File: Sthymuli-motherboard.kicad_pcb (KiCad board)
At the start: 4 copper layers, 153.6 x 66.2 mm, 196 parts, among them J1 USB_C_Receptacle_USB2.0_16P, J11 Conn_02x08_Counter_Clockwise, J12 Conn_02x08_Counter_Clockwise, J2 Conn_01x09, J3 Conn_01x03, J4 Conn_01x06, J8 Conn_02x08_Counter_Clockwise, Q1 Q_NMOS_Depletion_GSD, Q2 Q_NMOS_Depletion_GSD, Q3 Q_NMOS_Depletion_GSD, Q4 Q_NMOS_Depletion_GSD, Q5 Q_NMOS_Depletion_GSD, Q6 Q_NMOS_Depletion_GSD, Q7 PMOS, Q8 NX7002AK, Q9 NX7002AK, SW1 SW_Push, SW2 SW_Push, SW3 SW_Push, SW4 SW_Push, U1 ESP32-S3-WROOM-1, U10 74HC4051, U11 MCP6L01x-xOT, U12 74HC4051, U14 LSM6DS3, U15 ITR9909, U16 ITR9909, U2 AP2112K-3.3, U3 BQ76905RGRR, U4 AP62300WU, U5 BQ25713, U6 AP62300WU, U7 MCP23017_SO, U8 AP22913CN4, U9 IRM-H6xxT

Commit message: done routing + cleaning PCB
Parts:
- J1: footprint Connector_USB:USB_C_Receptacle_G-Switch_GT-USB-7010ASV -> sthymuli:USB_C_Receptacle_G-Switch_GT-USB-7010ASV
- U3: footprint Package_DFN_QFN:Texas_RGP0020H_VQFN-20-1EP_4x4mm_P0.5mm_EP2.4x2.4mm -> sthymuli:IC_BQ76905RGRR
- moved U1 0.09 mm to (102.2, 89.6)
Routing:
- net GND: track 695.8 -> 736.4 mm
- net Net-(U3-VC2): track 8.15 -> 11.2 mm
- net BMS_ALERT: track 57.3 -> 57.8 mm
- net Net-(U1-3V3): track 105.9 -> 106.4 mm

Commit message: regenerated output
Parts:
- added G***: LOGO, LOGO, B.Cu at (95.5, 91.8)
- added REF**: OSHW-Logo_19x20mm_SilkScreen, Symbol:OSHW-Logo_19x20mm_SilkScreen, B.Cu at (188.0, 112.5)
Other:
- board text added: "5V"
- board text added: "ACCEL_INT SDA VERT HORI DIN BAT+ BTN_DW 3V3"
- board text added: "EAST"
- board text added: "GND"
- board text added: "GPIO_1"
- board text added: "GPIO_2"
- board text added: "NC SDA VERT HOR DIN B+ DW 3V"
- board text added: "NC SDA VERT HORI DIN BAT+ BTN_DW 3V3"
- board text added: "SCL"
- board text added: "SCL IR_TRA_VERT TRA_HORI DOUT BAT- N_UP GND 5V"
- board text added: "SCL T_VE T_HO DO B- UP GD 5V"
- board text added: "SDA"
- board text added: "SOUTH"
- board text added: "WEST"
- board text added: "github.com/nathmo/Sthymuli-motherboard"
- board text added: "sthymuli motherboard V1.0 (2026) Nathann M Manuel BL"

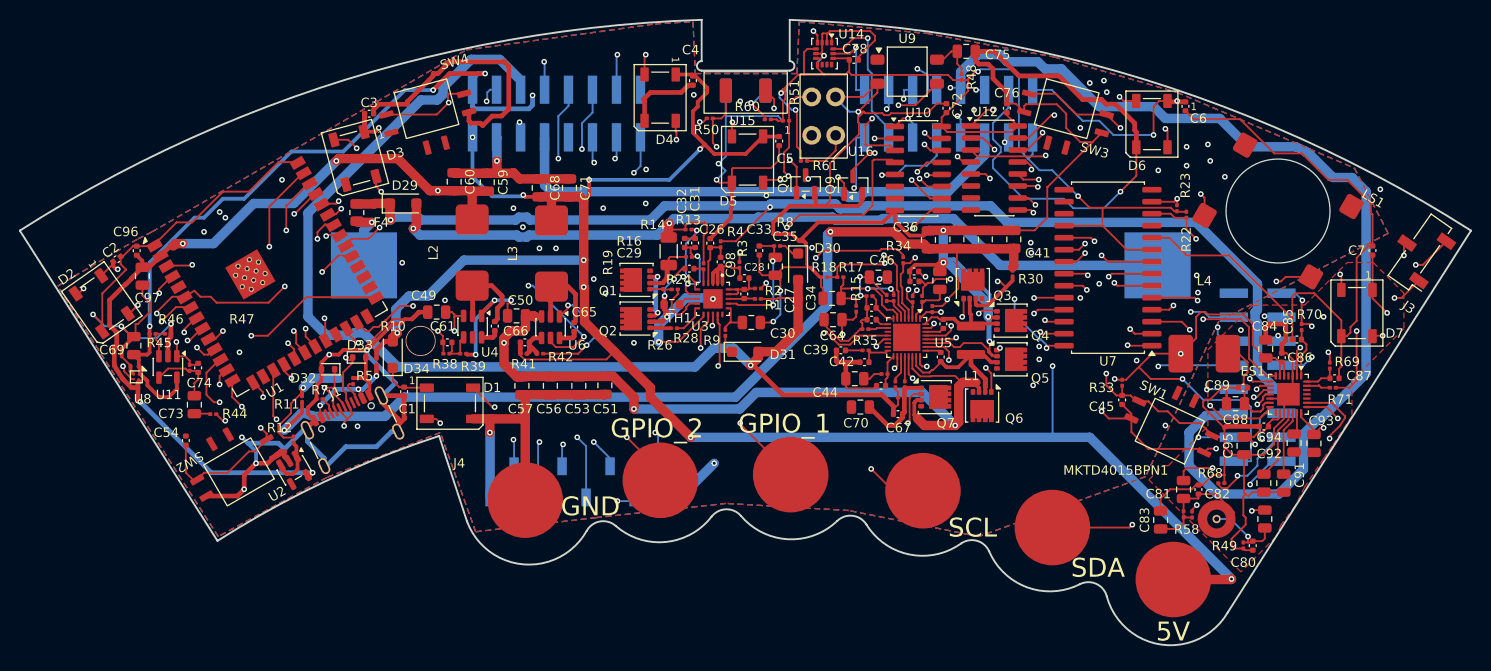
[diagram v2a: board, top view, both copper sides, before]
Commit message: slowly re routing the broken track
fixed resistor footprint
updated DRC checks
improved schematic readability
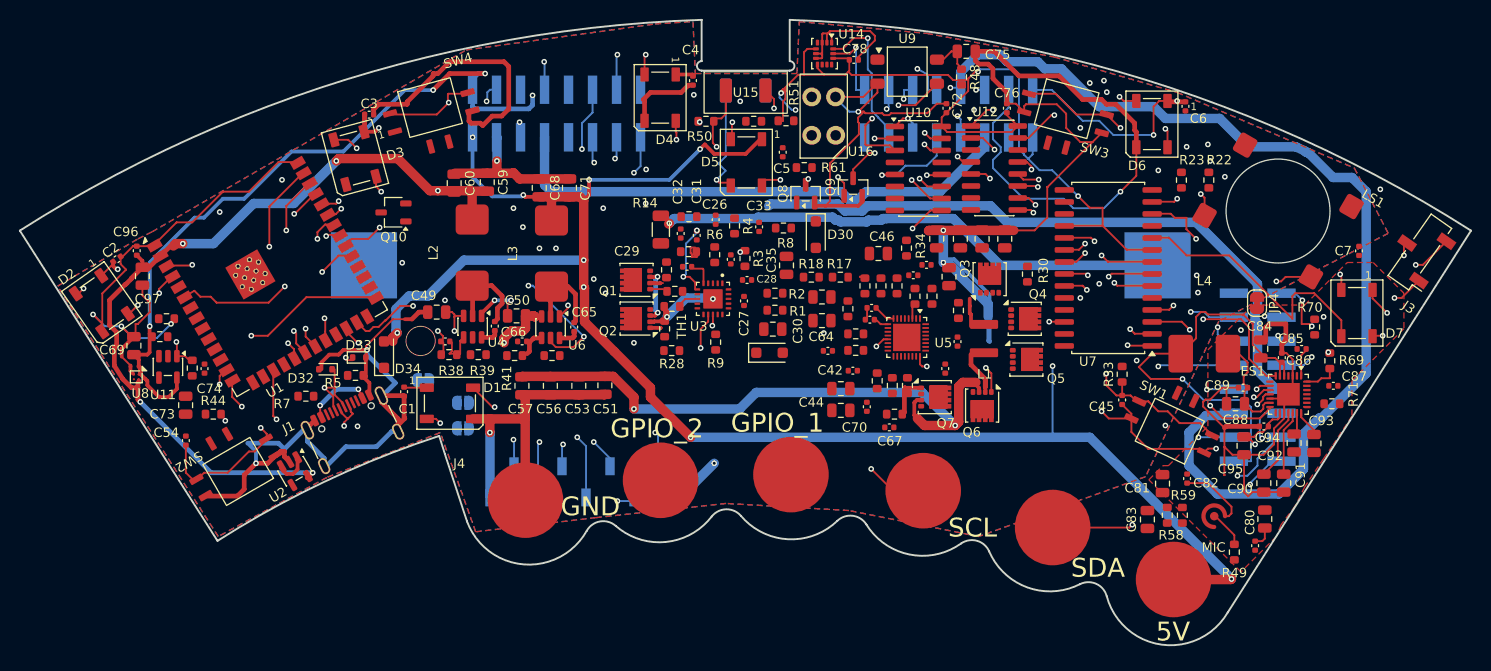
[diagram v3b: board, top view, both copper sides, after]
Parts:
- removed D29: D_Schottky, Diode_SMD:D_SOD-123F
- removed F4: Fuse, Resistor_SMD:R_0805_2012Metric
- removed R10, R12: OL, Capacitor_SMD:C_0201_0603Metric
- removed R11, R68: 0R, Capacitor_SMD:C_0201_0603Metric
- added JP1: SolderJumper_2_Bridged, Jumper:SolderJumper-2_P1.3mm_Bridged_RoundedPad1.0x1.5mm, B.Cu at (120.5, 103.7)
- added JP2: SolderJumper_2_Open, Jumper:SolderJumper-2_P1.3mm_Open_RoundedPad1.0x1.5mm, B.Cu at (124.7, 106.1)
- added JP3: SolderJumper_2_Open, Jumper:SolderJumper-2_P1.3mm_Open_RoundedPad1.0x1.5mm, B.Cu at (124.7, 108.8)
- added JP4: SolderJumper_2_Bridged, Jumper:SolderJumper-2_P1.3mm_Bridged_RoundedPad1.0x1.5mm, F.Cu at (208.7, 95.5)
- added Q10: Q_PMOS_GSD, Package_TO_SOT_SMD:TSOT-23, F.Cu at (117.3, 86.0)
- R1, R13, R15, R16, R17, R18, R19, R2, R20, R21, R22, R23, R24, R25, R26, R27, R28, R29, R3, R30, R31, R32, R33, R34, R35, R36, R37, R38, R39, R4, R40, R41, R42, R43, R44, R45, R46, R47, R48, R49, R5, R50, R51, R58, R59, R6, R60, R61, R69, R7, R70, R71, R8, R9: footprint Capacitor_SMD:C_0201_0603Metric -> Resistor_SMD:R_0603_1608Metric
- U7: value MCP23017_SO -> MCP23017x-x-SO
- moved R22 4.38 mm to (203.6, 82.5)
- moved D30 3.88 mm to (162.0, 88.3)
- moved R23 3.01 mm to (200.7, 82.5)
- moved R27 2.78 mm to (177.1, 96.3)
- moved C43 2.68 mm to (167.4, 106.5), turned to -90 degrees
- moved D31 2.58 mm to (157.1, 100.8)
- moved C26 2.55 mm to (151.4, 86.7)
- moved C33 2.50 mm to (156.0, 87.5)
- moved C46 2.50 mm to (168.6, 90.3)
- moved R14 2.44 mm to (145.6, 87.8)
- moved R4 2.44 mm to (153.4, 87.4)
- moved C52 2.40 mm to (177.0, 99.6)
- moved R28 2.39 mm to (146.8, 100.6)
- moved C30 2.38 mm to (157.4, 98.3)
- moved C81 2.31 mm to (198.7, 114.7)
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- renumbered MKTD4015BPN1 to MIC
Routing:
- net GND: track 736.4 -> 517.3 mm, vias 37 -> 20
- net WEST_BAT+: track 131.1 -> 0.00 mm, vias 1 -> 0
- net I2S_DOUT: track 126.9 -> 0.00 mm, vias 4 -> 0
- net I2S_MCLK: track 126.4 -> 0.00 mm, vias 2 -> 0
- net IR_MODULATION: track 113.8 -> 0.00 mm, vias 3 -> 0
- net Net-(JP1-B): track 109.8 -> 0.00 mm, vias 4 -> 0
- net ACC_A_INT1: track 107.5 -> 0.00 mm, vias 4 -> 0
- net ACC_B_INT1: track 90.8 -> 0.00 mm, vias 3 -> 0
- net +3V3: track 379.6 -> 300.6 mm, vias 17 -> 13
- net EXT_GPIO_1: track 78.6 -> 0.00 mm, vias 2 -> 0
- net EXT_GPIO_2: track 58.6 -> 0.00 mm, vias 2 -> 0
- net BMS_ALERT: track 57.8 -> 0.00 mm, vias 2 -> 0
- net EAST_BAT-: track 121.1 -> 68.1 mm, vias 2 -> 0
- net WEST_IR_REC_HORI: track 52.4 -> 0.00 mm, vias 2 -> 0
- net NORTH_BAT-: track 96.3 -> 54.5 mm, vias 2 -> 1
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
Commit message: 40 left
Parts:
- moved R44 0.70 mm to (98.2, 106.6)
- moved SW2 0.60 mm to (100.2, 112.5)
- moved C48 0.48 mm to (172.8, 92.6)
- moved U2 0.06 mm to (106.9, 113.3)
- renumbered MIC to MKTD4015BPN1
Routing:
- net I2S_MCLK: track 0.00 -> 123.0 mm, vias 0 -> 2
- net I2S_DOUT: track 0.00 -> 118.4 mm, vias 0 -> 2
- net ACC_A_INT1: track 0.00 -> 113.2 mm, vias 0 -> 3
- net IR_MODULATION: track 0.00 -> 105.9 mm, vias 0 -> 3
- net ACC_B_INT1: track 0.00 -> 97.6 mm, vias 0 -> 3
- net WEST_BAT+: track 0.00 -> 92.5 mm, vias 0 -> 7
- net GND: track 517.3 -> 605.3 mm, vias 20 -> 27
- net EXT_GPIO_1: track 0.00 -> 85.8 mm, vias 0 -> 3
- net Net-(JP1-B): track 0.00 -> 85.0 mm, vias 0 -> 3
- net +3V3: track 300.6 -> 372.3 mm, vias 13 -> 18
- net EXT_GPIO_2: track 0.00 -> 66.1 mm, vias 0 -> 2
- net BMS_ALERT: track 0.00 -> 65.5 mm, vias 0 -> 3
- net WEST_IR_REC_HORI: track 0.00 -> 56.4 mm, vias 0 -> 3
- net +5V: track 356.9 -> 399.2 mm, vias 17 -> 19
- net EAST_BAT-: track 68.1 -> 110.2 mm, vias 0 -> 3
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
